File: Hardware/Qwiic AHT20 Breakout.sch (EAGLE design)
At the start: 23 parts, among them J2 QWIIC_RIGHT_ANGLE, J3 PTH, J4 QWIIC_RIGHT_ANGLE, U2 AHT20QFN-6

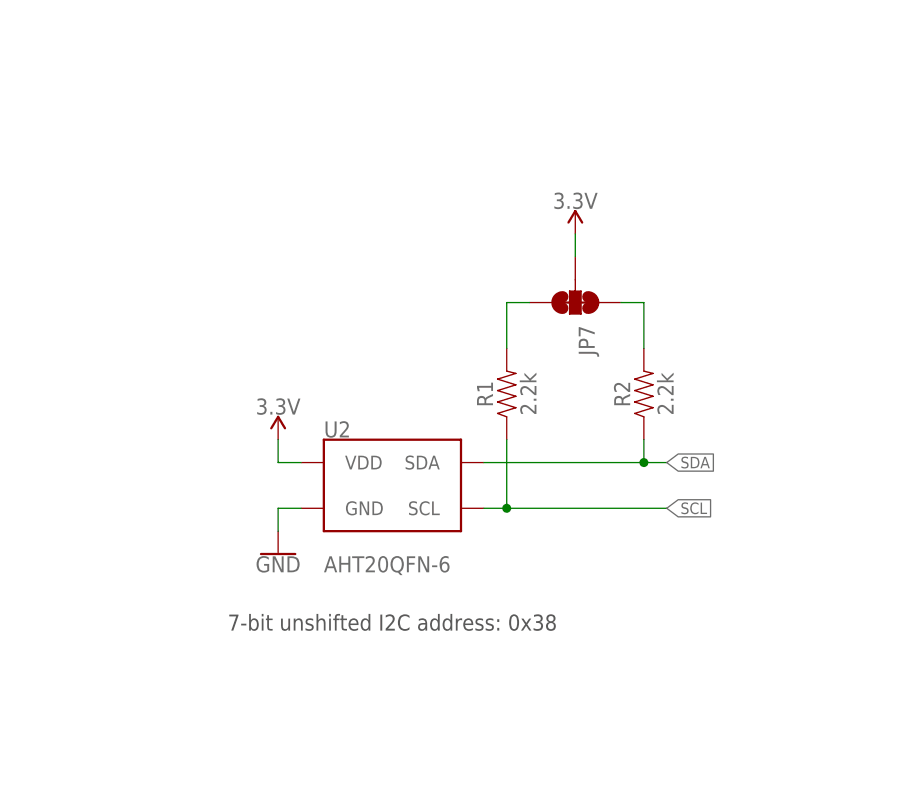
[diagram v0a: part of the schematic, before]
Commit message: Added NCD2400M to schematic
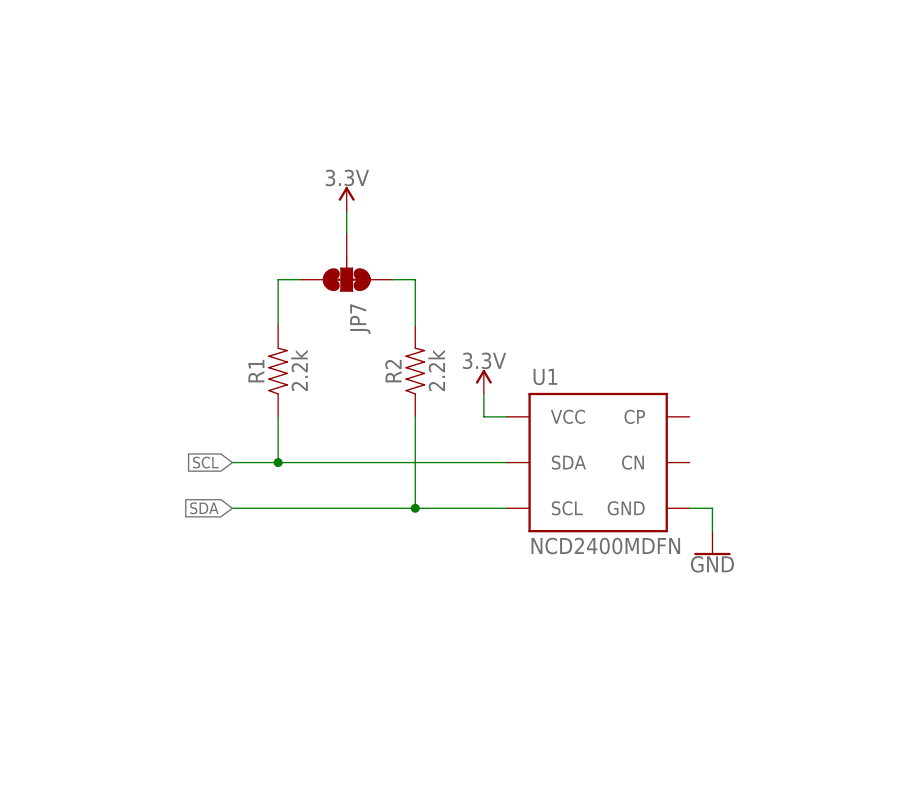
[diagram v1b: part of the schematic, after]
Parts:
- removed U2: AHT20QFN-6, AHT20:AHT20QFN-6
- added U1: NCD2400MDFN, SparkFun-Capacitors:NCD2400MDFN
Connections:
- net 3.3V: now also U1.VCC; no longer U2.VDD
- net GND: now also U1.GND; no longer U2.GND
- net SCL: now also U1.SDA; no longer U2.SCL
- net SDA: now also U1.SCL; no longer U2.SDA
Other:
- note removed: "7-bit unshifted I2C address: 0x38"
- moved on the sheet: JP7, R1, R2
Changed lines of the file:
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@@
 <?xml version="1.0" encoding="utf-8"?>
 <!DOCTYPE eagle SYSTEM "eagle.dtd">
-<eagle version="9.6.0">
+<eagle version="9.5.2">
 <drawing>
 <settings>
-<setting alwaysvectorfont="yes"/>
+<setting alwaysvectorfont="no"/>
 <setting keepoldvectorfont="yes"/>
 <setting verticaltext="up"/>
@@
 <part name="GND6" library="SparkFun-PowerSymbols" deviceset="GND" device=""/>
 <part name="LED" library="SparkFun-Jumpers" deviceset="JUMPER-SMT_2_NC_TRACE" device="_SILK" package3d_urn="urn:adsk.eagle:package:39281/1" value="JUMPER-SMT_2_NC_TRACE_SILK"/>
-<part name="U2" library="AHT20" deviceset="AHT20" device="QFN-6"/>
+<part name="U1" library="SparkFun-Capacitors" deviceset="NCD2400M" device="DFN"/>
 </parts>
 <sheets>
@@
 <plain>
 <text x="237.744" y="7.366" size="2.54" layer="94">x01</text>
-<text x="116.84" y="109.22" size="1.778" layer="97" align="center">7-bit unshifted I2C address: 0x38</text>
 <text x="38.608" y="114.046" size="1.778" layer="97">Power</text>
 <wire x1="0" y1="68.58" x2="248.92" y2="68.58" width="0.2032" layer="97" style="longdash"/>
@@
 <attribute name="VALUE" x="34.925" y="112.268" size="1.778" layer="96" font="vector" rot="R90" align="top-left"/>
 </instance>
-<instance part="R1" gate="G$1" x="129.54" y="134.62" smashed="yes" rot="R90">
-<attribute name="NAME" x="128.016" y="134.62" size="1.778" layer="95" font="vector" rot="R90" align="bottom-center"/>
-<attribute name="VALUE" x="131.064" y="134.62" size="1.778" layer="96" font="vector" rot="R90" align="top-center"/>
-</instance>
-<instance part="R2" gate="G$1" x="144.78" y="134.62" smashed="yes" rot="R90">
-<attribute name="NAME" x="143.256" y="134.62" size="1.778" layer="95" font="vector" rot="R90" align="bottom-center"/>
-<attribute name="VALUE" x="146.304" y="134.62" size="1.778" layer="96" font="vector" rot="R90" align="top-center"/>
-</instance>
-<instance part="JP7" gate="G$1" x="137.16" y="144.78" smashed="yes" rot="R270">
-<attribute name="NAME" x="137.541" y="142.24" size="1.778" layer="95" font="vector" rot="R270"/>
-</instance>
-<instance part="SUPPLY1" gate="G$1" x="104.14" y="129.54" smashed="yes">
-<attribute name="VALUE" x="104.14" y="132.334" size="1.778" layer="96" align="bottom-center"/>
-</instance>
-<instance part="SUPPLY2" gate="G$1" x="137.16" y="152.4" smashed="yes">
-<attribute name="VALUE" x="137.16" y="155.194" size="1.778" layer="96" align="bottom-center"/>
+<instance part="R1" gate="G$1" x="104.14" y="137.16" smashed="yes" rot="R90">
+<attribute name="NAME" x="102.616" y="137.16" size="1.778" layer="95" font="vector" rot="R90" align="bottom-center"/>
+<attribute name="VALUE" x="105.664" y="137.16" size="1.778" layer="96" font="vector" rot="R90" align="top-center"/>
+</instance>
+<instance part="R2" gate="G$1" x="119.38" y="137.16" smashed="yes" rot="R90">
+<attribute name="NAME" x="117.856" y="137.16" size="1.778" layer="95" font="vector" rot="R90" align="bottom-center"/>
+<attribute name="VALUE" x="120.904" y="137.16" size="1.778" layer="96" font="vector" rot="R90" align="top-center"/>
+</instance>
+<instance part="JP7" gate="G$1" x="111.76" y="147.32" smashed="yes" rot="R270">
+<attribute name="NAME" x="112.141" y="144.78" size="1.778" layer="95" font="vector" rot="R270"/>
+</instance>
+<instance part="SUPPLY1" gate="G$1" x="127" y="134.62" smashed="yes">
+<attribute name="VALUE" x="127" y="137.414" size="1.778" layer="96" align="bottom-center"/>
+</instance>
+<instance part="SUPPLY2" gate="G$1" x="111.76" y="154.94" smashed="yes">
+<attribute name="VALUE" x="111.76" y="157.734" size="1.778" layer="96" align="bottom-center"/>
 </instance>
 <instance part="C1" gate="G$1" x="63.5" y="124.46" smashed="yes">
@@
 <attribute name="VALUE" x="63.5" y="116.586" size="1.778" layer="96" align="top-center"/>
 </instance>
-<instance part="GND3" gate="1" x="104.14" y="116.84" smashed="yes">
-<attribute name="VALUE" x="104.14" y="116.586" size="1.778" layer="96" align="top-center"/>
+<instance part="GND3" gate="1" x="152.4" y="116.84" smashed="yes">
+<attribute name="VALUE" x="152.4" y="116.586" size="1.778" layer="96" align="top-center"/>
 </instance>
 <instance part="GND4" gate="1" x="76.2" y="38.1" smashed="yes">
@@
 <attribute name="VALUE" x="35.56" y="137.16" size="1.778" layer="96" font="vector" rot="R90" align="top-left"/>
 </instance>
-<instance part="U2" gate="G$1" x="116.84" y="124.46" smashed="yes">
-<attribute name="NAME" x="109.22" y="129.794" size="1.778" layer="95" font="vector"/>
-<attribute name="VALUE" x="109.22" y="116.586" size="1.778" layer="96" font="vector" align="top-left"/>
+<instance part="U1" gate="U1" x="139.7" y="127" smashed="yes">
+<attribute name="NAME" x="132.334" y="135.636" size="1.778" layer="95"/>
+<attribute name="VALUE" x="132.08" y="116.84" size="1.778" layer="95"/>
 </instance>
 </instances>
@@
 </segment>
 <segment>
-<pinref part="SUPPLY1" gate="G$1" pin="3.3V"/>
-<wire x1="106.68" y1="127" x2="104.14" y2="127" width="0.1524" layer="91"/>
-<wire x1="104.14" y1="127" x2="104.14" y2="129.54" width="0.1524" layer="91"/>
-<pinref part="U2" gate="G$1" pin="VDD"/>
-</segment>
-<segment>
 <pinref part="JP7" gate="G$1" pin="2"/>
-<wire x1="137.16" y1="149.86" x2="137.16" y2="152.4" width="0.1524" layer="91"/>
+<wire x1="111.76" y1="152.4" x2="111.76" y2="154.94" width="0.1524" layer="91"/>
 <pinref part="SUPPLY2" gate="G$1" pin="3.3V"/>
 </segment>
@@
 <wire x1="33.02" y1="147.32" x2="33.02" y2="144.78" width="0.1524" layer="91"/>
 </segment>
+<segment>
+<pinref part="U1" gate="U1" pin="VCC"/>
+<wire x1="129.54" y1="132.08" x2="127" y2="132.08" width="0.1524" layer="91"/>
+<pinref part="SUPPLY1" gate="G$1" pin="3.3V"/>
+<wire x1="127" y1="132.08" x2="127" y2="134.62" width="0.1524" layer="91"/>
+</segment>
 </net>
 <net name="SCL" class="0">
@@
 </segment>
 <segment>
+<wire x1="129.54" y1="127" x2="104.14" y2="127" width="0.1524" layer="91"/>
+<label x="99.06" y="127" size="1.27" layer="95" rot="R180" xref="yes"/>
+<pinref part="U1" gate="U1" pin="SDA"/>
 <pinref part="R1" gate="G$1" pin="1"/>
-<wire x1="129.54" y1="129.54" x2="129.54" y2="121.92" width="0.1524" layer="91"/>
-<wire x1="129.54" y1="121.92" x2="127" y2="121.92" width="0.1524" layer="91"/>
-<wire x1="129.54" y1="121.92" x2="147.32" y2="121.92" width="0.1524" layer="91"/>
-<junction x="129.54" y="121.92"/>
-<label x="147.32" y="121.92" size="1.27" layer="95" xref="yes"/>
-<pinref part="U2" gate="G$1" pin="SCL"/>
+<wire x1="104.14" y1="127" x2="99.06" y2="127" width="0.1524" layer="91"/>
+<wire x1="104.14" y1="132.08" x2="104.14" y2="127" width="0.1524" layer="91"/>
+<junction x="104.14" y="127"/>
 </segment>
 </net>
@@
 </segment>
 <segment>
+<wire x1="99.06" y1="121.92" x2="119.38" y2="121.92" width="0.1524" layer="91"/>
+<label x="99.06" y="121.92" size="1.27" layer="95" rot="R180" xref="yes"/>
+<pinref part="U1" gate="U1" pin="SCL"/>
 <pinref part="R2" gate="G$1" pin="1"/>
-<wire x1="144.78" y1="129.54" x2="144.78" y2="127" width="0.1524" layer="91"/>
-<wire x1="144.78" y1="127" x2="127" y2="127" width="0.1524" layer="91"/>
-<wire x1="144.78" y1="127" x2="147.32" y2="127" width="0.1524" layer="91"/>
-<junction x="144.78" y="127"/>
-<label x="147.32" y="127" size="1.27" layer="95" xref="yes"/>
-<pinref part="U2" gate="G$1" pin="SDA"/>
+<wire x1="119.38" y1="121.92" x2="129.54" y2="121.92" width="0.1524" layer="91"/>
+<wire x1="119.38" y1="132.08" x2="119.38" y2="121.92" width="0.1524" layer="91"/>
+<junction x="119.38" y="121.92"/>
 </segment>
 </net>
@@
 <segment>
 <pinref part="R1" gate="G$1" pin="2"/>
-<wire x1="129.54" y1="139.7" x2="129.54" y2="144.78" width="0.1524" layer="91"/>
+<wire x1="104.14" y1="142.24" x2="104.14" y2="147.32" width="0.1524" layer="91"/>
 <pinref part="JP7" gate="G$1" pin="3"/>
-<wire x1="129.54" y1="144.78" x2="132.08" y2="144.78" width="0.1524" layer="91"/>
+<wire x1="104.14" y1="147.32" x2="106.68" y2="147.32" width="0.1524" layer="91"/>
 </segment>
 </net>
@@
 <pinref part="R2" gate="G$1" pin="2"/>
 <pinref part="JP7" gate="G$1" pin="1"/>
-<wire x1="144.78" y1="139.7" x2="144.78" y2="144.78" width="0.1524" layer="91"/>
-<wire x1="144.78" y1="144.78" x2="142.24" y2="144.78" width="0.1524" layer="91"/>
+<wire x1="119.38" y1="142.24" x2="119.38" y2="147.32" width="0.1524" layer="91"/>
+<wire x1="119.38" y1="147.32" x2="116.84" y2="147.32" width="0.1524" layer="91"/>
 </segment>
 </net>
@@
 <wire x1="63.5" y1="119.38" x2="63.5" y2="121.92" width="0.1524" layer="91"/>
 <pinref part="GND2" gate="1" pin="GND"/>
-</segment>
-<segment>
-<wire x1="106.68" y1="121.92" x2="104.14" y2="121.92" width="0.1524" layer="91"/>
-<wire x1="104.14" y1="121.92" x2="104.14" y2="119.38" width="0.1524" layer="91"/>
-<pinref part="GND3" gate="1" pin="GND"/>
-<pinref part="U2" gate="G$1" pin="GND"/>
 </segment>
 <segment>
@@
 <pinref part="GND6" gate="1" pin="GND"/>
 </segment>
-</net>
+<segment>
+<pinref part="U1" gate="U1" pin="GND"/>
+<wire x1="149.86" y1="121.92" x2="152.4" y2="121.92" width="0.1524" layer="91"/>
+<pinref part="GND3" gate="1" pin="GND"/>
+<wire x1="152.4" y1="121.92" x2="152.4" y2="119.38" width="0.1524" layer="91"/>
+</segment>
+</net>
